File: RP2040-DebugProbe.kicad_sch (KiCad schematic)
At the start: 60 parts, among them J1 CONN_MCU_JTAG, J10 CONN_USB, J2 CONN_MCU_UART, J3 CONN_DBG_COMB, J4 CONN_3V3_JUMPER, J7 CONN_DBG_JTAG, SW1 BOOTSEL, U1 W25Q128JVS, U2 RP2040, U3 74AUP1T17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

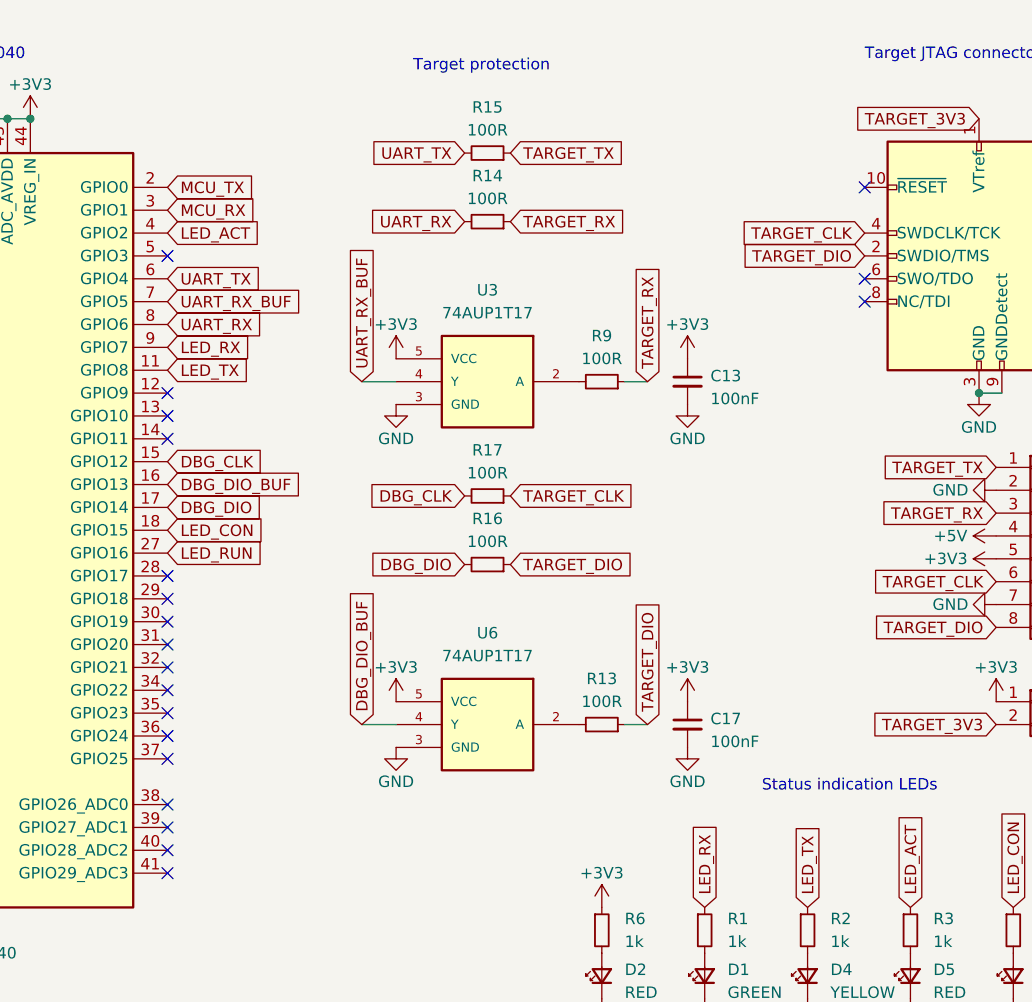
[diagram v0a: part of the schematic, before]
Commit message: Added target reset line on GPIO 10
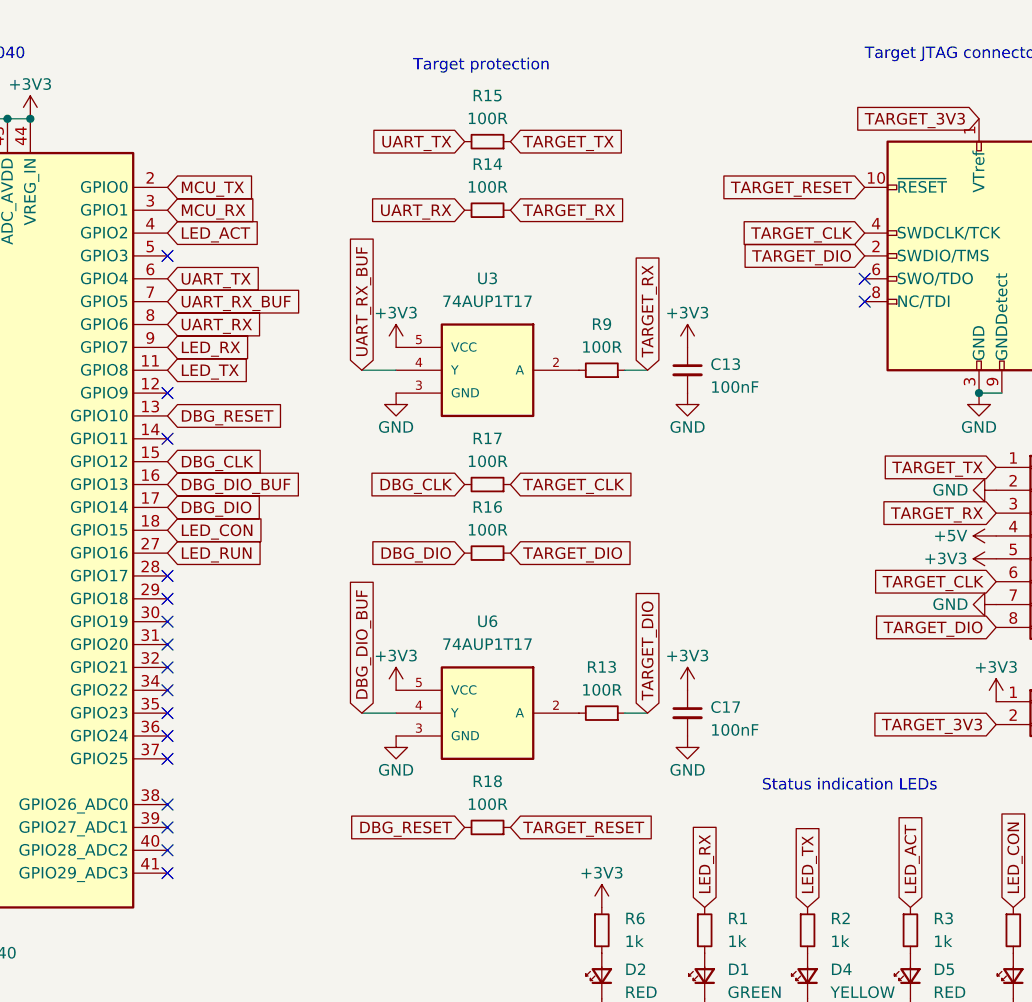
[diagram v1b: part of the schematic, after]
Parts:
- added R18: 100R, Resistor_SMD:R_0402_1005Metric, symbol Device:R_Small
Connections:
- net TARGET_RESET: now reaches J7.10 (~{RESET})
- net TARGET_RESET: now also R18.1
- net DBG_RESET: now reaches U2.13 (GPIO10)
- net DBG_RESET: now also R18.2
- no-connect marks 24 -> 22
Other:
- moved on the sheet: C13, C17, R13, R14, R15, R16, R17, R9, U3, U6

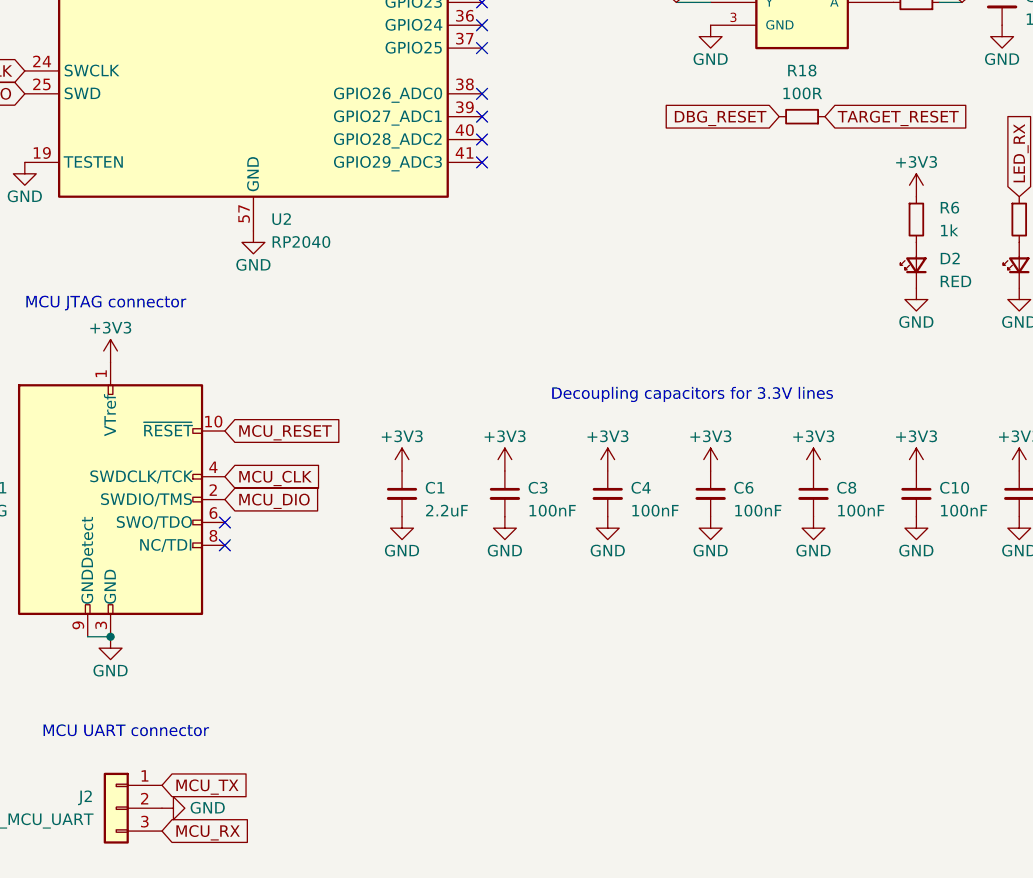
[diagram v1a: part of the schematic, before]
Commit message: Added host side protection resistors
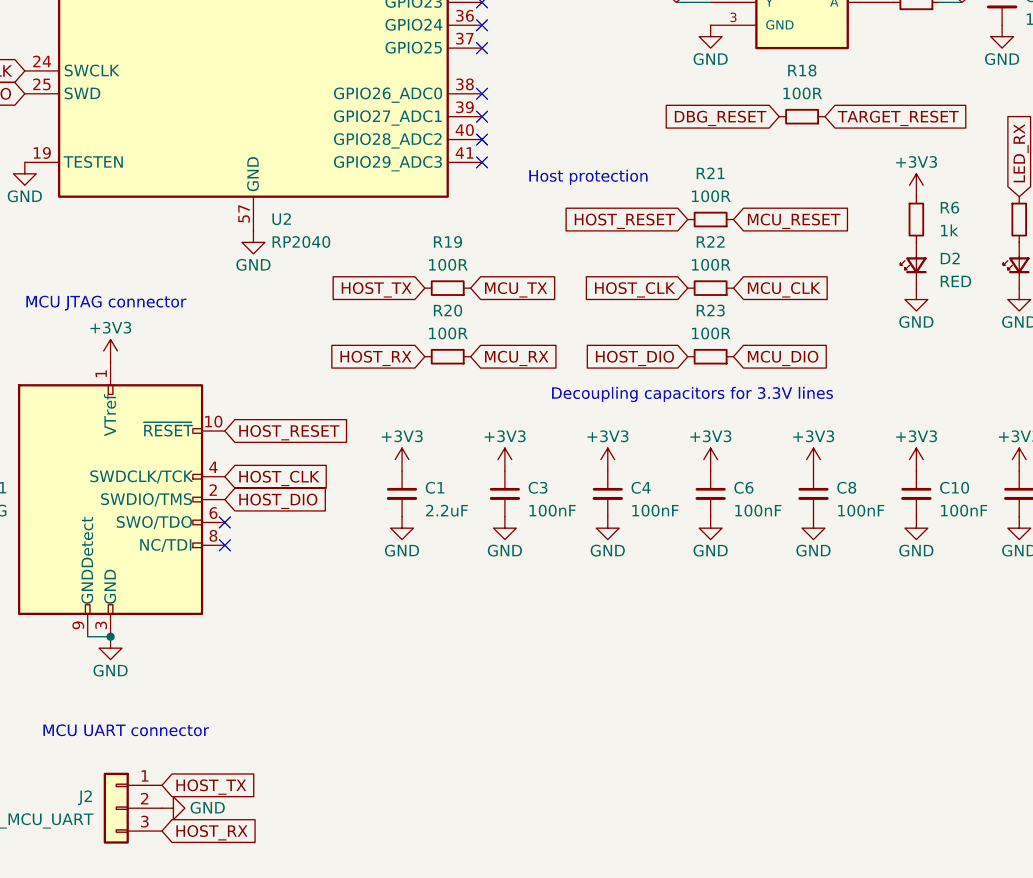
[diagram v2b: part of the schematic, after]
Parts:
- added R19, R20, R21, R22, R23: 100R, Resistor_SMD:R_0402_1005Metric, symbol Device:R_Small
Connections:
- net MCU_CLK: now also R22.1; no longer J1.4 (SWDCLK/TCK)
- net MCU_DIO: now also R23.1; no longer J1.2 (SWDIO/TMS)
- net MCU_RESET: now also R21.1; no longer J1.10 (~{RESET})
- net MCU_RX: now also R20.1; no longer J2.3 (Pin_3)
- net MCU_TX: now also R19.1; no longer J2.1 (Pin_1)
- new net HOST_CLK: J1.4 (SWDCLK/TCK), R22.2
- new net HOST_DIO: J1.2 (SWDIO/TMS), R23.2
- new net HOST_RESET: J1.10 (~{RESET}), R21.2
- new net HOST_RX: J2.3 (Pin_3), R20.2
- new net HOST_TX: J2.1 (Pin_1), R19.2
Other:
- note added: "Host protection"
